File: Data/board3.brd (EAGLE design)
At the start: 70 x 67.5 mm, 69 parts, among them Q1 16MHz, U1 ACPL224, U10 PIC18F46K22-I/PT, U11 MAX3232CSE, U12 ACPL224, U13 VO1400, U14 VO1400, U15 VO1400, U16 VO1400, U17 VO1400, U18 VO1400, U2 ACPL224, U3 ACPL224, U4 ACPL224, U5 VO1400, U6 VO1400, U7 VO1400, U8 VO1400, U9 MCP17033302I/MB, X1 2514-5, X2 2514-5

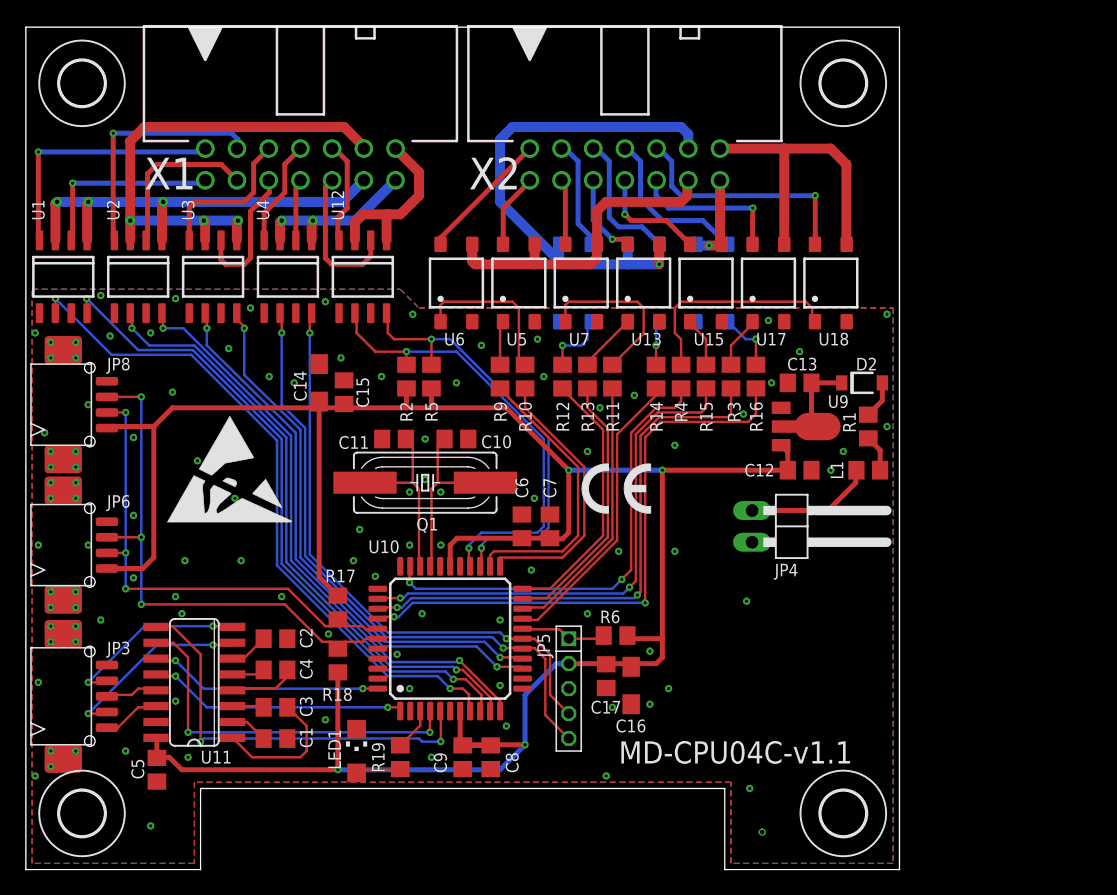
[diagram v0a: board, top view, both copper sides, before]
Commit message: Millores en la deteccio d'error del importador eagle
Signed-off-by: Rafael Serrano <rsr.private@gmail.com>
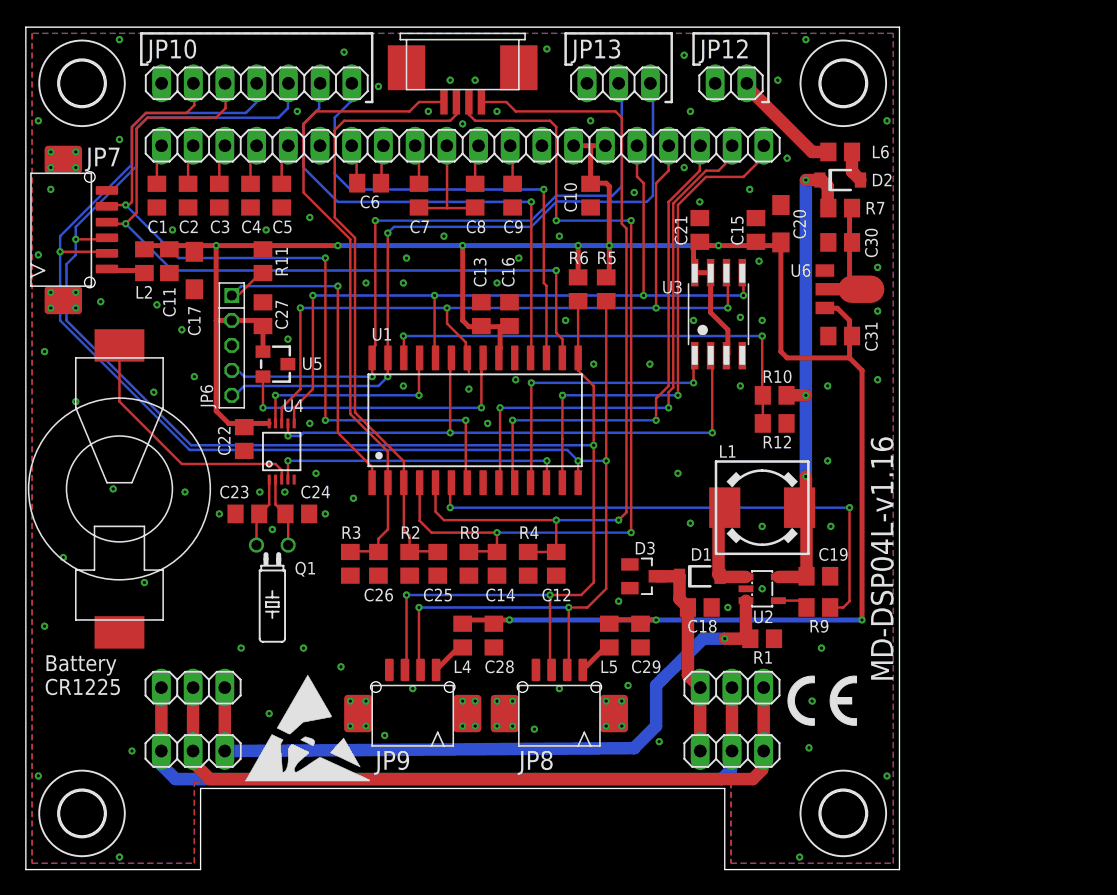
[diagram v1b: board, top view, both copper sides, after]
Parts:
- removed LED1: GREEN, led:CHIPLED_1206
- removed R13, R14, R15, R16, R19: 270, rcl:R0805
- removed R17, R18: 1K5, rcl:R0805
- removed U$10, U$9: (no value), holes:3,6
- removed U10: PIC18F46K22-I/PT, microchip-pic:TQFP44
- removed U11: MAX3232CSE, maxim:SO16
- removed U12: ACPL224, optoacopladores:SO08
- removed U13, U14, U15, U16, U17, U18, U7, U8: VO1400, optoacopladores:SOP04
- removed U9: MCP17033302I/MB, microchip-analog:SOT89
- removed X1, X2: 2514-5, con-3m:PAK100/2500-5-14
- added BAT1: CR1225, bateries:SMTU-1225-1
- added C18: 1u/25V, rcl:C0805
- added C19: 10u, rcl:C0805
- added C20: 10u/6.3V, rcl:SMC_A
- added C21, C22, C25, C26, C27, C28, C29: 100n, rcl:C0805
- added C23, C24: 8p, rcl:C0805
- added C30, C31: 4u7, rcl:C0805
- added D1: MBR0540, diode:SOD123FL
- added D3: BZX84C24, diode:SOT23
- added JP1: (no value), pinhead:1X20
- added JP10: (no value), pinhead:1X07
- added JP11: (no value), te-connector-fpc:FPC-ZB4-1MM
- added JP12: (no value), pinhead:1X02
- added JP13, JP2: (no value), pinhead:1X03
- added JP7: DF13-1X6-SMD-90-E, hirose-df13:1X6-SMD-90-E
- added JP9: DF13-1X4-SMD-90-E, hirose-df13:1X4-SMD-90-E
- added L2, L4, L5, L6: 600R, rcl-2:L0805
- added R7: 5R, rcl:R0805
- added R8: 47k, rcl:R0805
- added U$4: (no value), holes:3,6
- added U$5: (no value), logo:CE-4MM
- C1, C2, C3, C4, C5, C7, C9: value 100n -> 1u/25V
- C10, C11: value 22p -> 100n
- C12, C13: value 4u7 -> 100n
- C14: value 10u -> 100n; device rcl:SMC_A -> rcl:C0805
- C16: value 10u -> 10n; device rcl:SMC_A -> rcl:C0805
- C17: value 100n -> 10u/6.3V; device rcl:C0805 -> rcl:SMC_A
- C6, C8: value 10n -> 1u/25V
- JP3: value DF13-1X5-SMD-90-E -> (none); device hirose-df13:1X5-SMD-90-E -> pinhead:1X03
- JP4: device pinhead:1X02/90 -> pinhead:1X03
- JP5: value ICSP -> (none); device pinhead200:1X05-2MM -> pinhead:1X03
- JP6: value DF13-1X4-SMD-90-E -> PINHD-1X5-2MM; device hirose-df13:1X4-SMD-90-E -> pinhead200:1X05-2MM
- L1: value 600R -> (none); device rcl-2:L0805 -> inductors:DR73
- Q1: value 16MHz -> 32Khz; device crystal:SM49 -> crystal:TC26H
- R1: value 5R1 -> 6R98
- R10, R9: value 270 -> 4K7
- R11: value 270 -> 10K
- R12: value 270 -> 1K5
- R2: value 10K -> 47k
- R3, R4: value 270 -> 47k
- R5, R6: value 10K -> 1K5
- U$1: device logo:CE-4MM -> holes:3,6
- U$2: device logo:ESD_10.00 -> holes:3,6
- U$6: device holes:3,6 -> logo:ESD_10.00
- U1: value ACPL224 -> PIC18F26K22-I/SO; device optoacopladores:SO08 -> microchip-pic:SO28W
- U2: value ACPL224 -> (none); device optoacopladores:SO08 -> onsemiconductor:SOT23-5L
- U3: value ACPL224 -> 25LC1024-I/SM; device optoacopladores:SO08 -> microchip-smem:SO08M
- U4: value ACPL224 -> MCP79520-I/MS; device optoacopladores:SO08 -> microchip-rtc:SO10
- U5: value VO1400 -> TC1047; device optoacopladores:SOP04 -> microchip-analog:TO236
- U6: value VO1400 -> MCP17033302I/MB; device optoacopladores:SOP04 -> microchip-analog:SOT89
- moved U$6 73.8 mm to (17.5, 7.00)
- moved U2 55.9 mm to (59.0, 22.5), turned to 270 degrees
- moved U$1 52.8 mm to (4.50, 63.0)
- moved JP4 51.8 mm to (13.4, 9.50), turned to 0 degrees
- moved JP3 50.2 mm to (56.6, 9.50), turned to 0 degrees
- moved C5 47.1 mm to (20.5, 54.0)
- moved C17 46.3 mm to (13.5, 48.0), turned to 270 degrees
- moved C9 45.2 mm to (39.0, 54.0)
- moved C8 45.0 mm to (36.0, 54.0), turned to 270 degrees
- moved C1 44.5 mm to (10.5, 54.0), turned to 90 degrees
- moved JP8 42.0 mm to (42.8, 16.0), turned to 180 degrees
- moved C3 41.2 mm to (15.5, 54.0), turned to 90 degrees
- moved U3 40.6 mm to (55.5, 44.5), turned to 0 degrees
- moved C4 38.1 mm to (18.0, 54.0), turned to 90 degrees
- moved C2 36.2 mm to (13.0, 54.0), turned to 90 degrees
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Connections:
- removed net I-COM0: U1.1, U1.3, U2.1, X1.11
- removed net I-COM1: U2.3, U3.1, U3.3, X1.12
- removed net I-COM2: U4.1, U4.3, X1.13
- removed net I-COM3: U12.1, U12.3, X1.14
- removed net I0: U1.2, X1.1
- removed net I1: U1.4, X1.2
- removed net I2: U2.2, X1.3
- removed net I3: U2.4, X1.4
- removed net I4: U3.2, X1.5
- removed net I5: U3.4, X1.6
- removed net I6: U4.2, X1.7
- removed net I7: U4.4, X1.8
- removed net I8: U12.2, X1.9
- removed net I9: U12.4, X1.10
- removed net IN0: U1.8, U10.9
- removed net IN1: U1.6, U10.8
- removed net IN2: U10.11, U2.8
- removed net IN3: U10.10, U2.6
- removed net IN4: U10.15, U3.8
- removed net IN5: U10.14, U3.6
- removed net IN6/PGD: JP5.4, U10.17, U4.8
- removed net IN7/PGC: JP5.5, U10.16, U4.6
- removed net IN8: R5.1, U10.25, U12.8
- removed net IN9: R2.1, U10.26, U12.6
- removed net LED: R19.2, U10.3
- removed net N$30: C4.2, U11.4
- removed net N$33: C4.1, U11.5
- removed net N$34: C1.1, U11.2
- removed net N$35: C2.1, U11.6
- removed net N$36: C11.2, Q1.2, U10.31
- removed net N$51: R15.2, U15.1
- removed net N$52: R13.2, U13.1
- removed net N$53: R14.2, U14.1
- removed net N$54: R16.2, U16.1
- removed net O-COM0: U5.3, U6.3, U7.3, X2.11
- removed net O-COM1: U13.3, U14.3, U8.3, X2.12
- removed net O-COM2: U15.3, U16.3, X2.13
- removed net O-COM3: U17.3, U18.3, X2.14
- removed net O0: U5.4, X2.1
- removed net O1: U6.4, X2.2
- removed net O2: U7.4, X2.3
- removed net O3: U8.4, X2.4
- removed net O4: U13.4, X2.5
- removed net O5: U14.4, X2.6
- removed net O6: U15.4, X2.7
- removed net O7: U16.4, X2.8
- removed net O8: U17.4, X2.9
- removed net O9: U18.4, X2.10
- removed net OUT0: R9.1, U10.24
- removed net OUT1: R10.1, U10.23
- removed net OUT2: R11.1, U10.20
- removed net OUT3: R12.1, U10.22
- removed net OUT4: R13.1, U10.21
- removed net OUT5: R14.1, U10.19
- removed net OUT6: R15.1, U10.35
- removed net OUT7: R16.1, U10.37
- removed net OUT8: R3.1, U10.36
- removed net OUT9: R4.1, U10.32
- removed net SCL2: JP6.2, JP8.2, R17.1, U10.38
- removed net SDA2: JP6.3, JP8.3, R18.1, U10.39
- new net +5V: C19.1, D2.C, L1.1, R10.2, R7.2, U2.5
- new net A+: C12.1, JP11.1, R4.2, U1.5
- new net A-: C25.1, JP11.3, R2.2, U1.3
- new net A0-DSP: JP1.18, U1.10
- new net B+: C14.1, JP11.2, R8.2, U1.4
- new net B-: C26.1, JP11.4, R3.2, U1.2
- new net BK_EN: R9.2, U1.6
- new net CS-DSP: JP1.20, U1.13
- new net CS-MEM: U1.11, U3.1
- new net CS-RTC: U1.12, U4.4
- new net MFP-RTC: U1.25, U4.9
- new net MISO: U1.23, U3.2, U4.7
- new net MOSI: JP1.16, U1.24, U3.5, U4.6
- new net N$10: C7.2, C8.2, JP1.10
- new net N$11: C8.1, JP1.11
- new net N$12: C9.2, JP1.12
- new net N$19: D1.A, L1.2, U2.1
- new net N$21: JP7.1, L2.2
- new net N$24: D2.A, L6.2
- new net N$27: C30.1, R7.1, U6.2, U6.2@1
- new net N$9: C7.1, JP1.9
- new net RST-DSP: JP1.19, U1.9
- new net SCK: JP1.17, U1.22, U3.6, U4.8
- new net SCL/SCK: JP10.4, JP7.2, JP8.2, JP9.2, R5.1, U1.14
- new net SDA/SDI: JP10.3, JP7.3, JP8.3, JP9.3, R6.1, U1.15
- new net SDO: JP10.5, JP7.4, U1.16
- new net SS: JP10.6, JP7.5, U1.7
- new net VPOWER: R10.1, R12.2, U1.26
- new net VTEMP: U1.21, U5.2
- net GND: now also BAT1.NEG, C1.1, C10.2, C11.2, C14.2, C15.2, C16.2, C17.-, C18.2, C19.2, C2.1, C20.-, C21.2, C22.2, C23.2, C24.2, C25.2, C26.2, C27.2, C28.2, C29.2, C3.1, C30.2, C31.2, C4.1, D3.1, JP1.13, JP1.6, JP10.7, JP12.2, JP13.3, JP6.3, JP7.6, JP9.4, R1.1, R12.1, R2.1, R3.1, R4.1, R8.1, U1.19, U1.8, U2.2, U3.4, U5.3, U6.1; no longer C1.2, C10.1, C11.1, C14.-, C15.1, C16.-, C17.1, C2.2, C6.1, C7.1, C8.1, JP3.5, JP4.2, JP5.3, JP6.4, LED1.C, U1.5, U1.7, U10.29, U10.6, U11.15, U12.5, U12.7, U13.2, U14.2, U15.2, U16.2, U17.2, U18.2, U2.5, U2.7, U3.5, U3.7, U4.7, U5.2, U6.2, U7.2, U8.2, U9.1
- net N$1: now also C1.2, JP1.1; no longer R3.2, U17.1
- net N$13: now also JP2.2, JP4.1, JP5.1; no longer U11.7
- net N$14: now also JP4.3, JP5.3, R1.2, U2.3; no longer JP3.3, U11.13
- net N$15: now also BAT1.POS, U4.3; no longer JP3.4, U11.8
- net N$16: now also C18.1, D1.C, D3.3, JP2.1, JP3.1; no longer C3.2, U11.1
- net N$17: now also C23.1, Q1.2, U4.1; no longer R9.2, U5.1
- net N$18: now also C24.1, Q1.1, U4.2; no longer R10.2, U6.1
- net N$2: now also C2.2, JP1.2; no longer JP4.1, L1.2
- net N$22: now also JP12.1, L6.1; no longer LED1.A, R19.1
- net N$25: now also JP9.1, L4.2; no longer R11.2, U7.1
- net N$26: now also JP8.1, L5.2; no longer R12.2, U8.1
- net N$29: now also R9.1, U2.4; no longer C3.1, U11.3
- net N$3: now also C3.2, JP1.3; no longer L1.1, R1.1
- net N$4: now also C4.2, JP1.4; no longer JP3.1, U11.14
- net N$5: now also C5.2, JP1.5; no longer C13.1, D2.C, U9.2, U9.2@1
- net N$6: now also JP2.3, JP3.3, JP4.2, JP5.2; no longer R4.2, U18.1
- net N$7: now also C6.2, JP1.7; no longer D2.A, R1.2
- net N$8: now also C6.1, JP1.8; no longer C10.2, Q1.1, U10.30
- net RX1: now also JP10.2, U1.18; no longer U10.1, U11.12
- net RX2: now also JP13.2, JP6.4, U1.28; no longer U10.5, U11.9
- net TX1: now also JP10.1, U1.17; no longer U10.44, U11.11
- net TX2: now also JP13.1, JP6.5, U1.27; no longer U10.4, U11.10
- net VCC: now also C10.1, C11.1, C13.1, C15.1, C16.1, C17.+, C20.+, C21.1, C22.1, C27.1, C28.1, C29.1, C31.1, JP1.14, JP1.15, JP6.2, L2.1, L4.1, L5.1, R11.2, U1.20, U3.3, U3.7, U3.8, U4.10, U5.1, U6.3; no longer C12.1, C14.+, C15.2, C16.+, C17.2, C5.2, C6.2, C7.2, C8.2, C9.2, JP5.2, JP6.1, JP8.1, R17.2, R18.2, R2.2, U10.28, U10.7, U11.16, U9.3
- net VPP: now also JP6.1, R11.1, U1.1; no longer JP5.1, R6.1, U10.18
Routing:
- net SDA/SDI: track 0.00 -> 133.5 mm, vias 0 -> 4
- net SCL/SCK: track 0.00 -> 132.9 mm, vias 0 -> 5
- net B+: track 0.00 -> 71.2 mm, vias 0 -> 4
- net SCK: track 0.00 -> 67.4 mm, vias 0 -> 4
- net A+: track 0.00 -> 66.5 mm, vias 0 -> 2
- net MOSI: track 0.00 -> 64.5 mm, vias 0 -> 4
- net SS: track 0.00 -> 62.7 mm, vias 0 -> 4
- net SDO: track 0.00 -> 62.6 mm, vias 0 -> 2
- net IN1: track 54.7 -> 0.00 mm, vias 2 -> 0
- net IN0: track 53.4 -> 0.00 mm, vias 2 -> 0
- net B-: track 0.00 -> 52.3 mm
- net N$14: track 4.24 -> 55.9 mm, vias 0 -> 1
- net A-: track 0.00 -> 50.7 mm
- net IN7/PGC: track 50.7 -> 0.00 mm, vias 2 -> 0
- net IN3: track 50.3 -> 0.00 mm, vias 2 -> 0
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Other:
- board text added: "Battery CR1225"
- board text added: "MD-DSP04L-v1.16"
- board text removed: "MD-CPU04C-v1.1"

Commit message: Implementacio GetOutline per l'element regio.
Signed-off-by: Rafael Serrano <rsr.private@gmail.com>
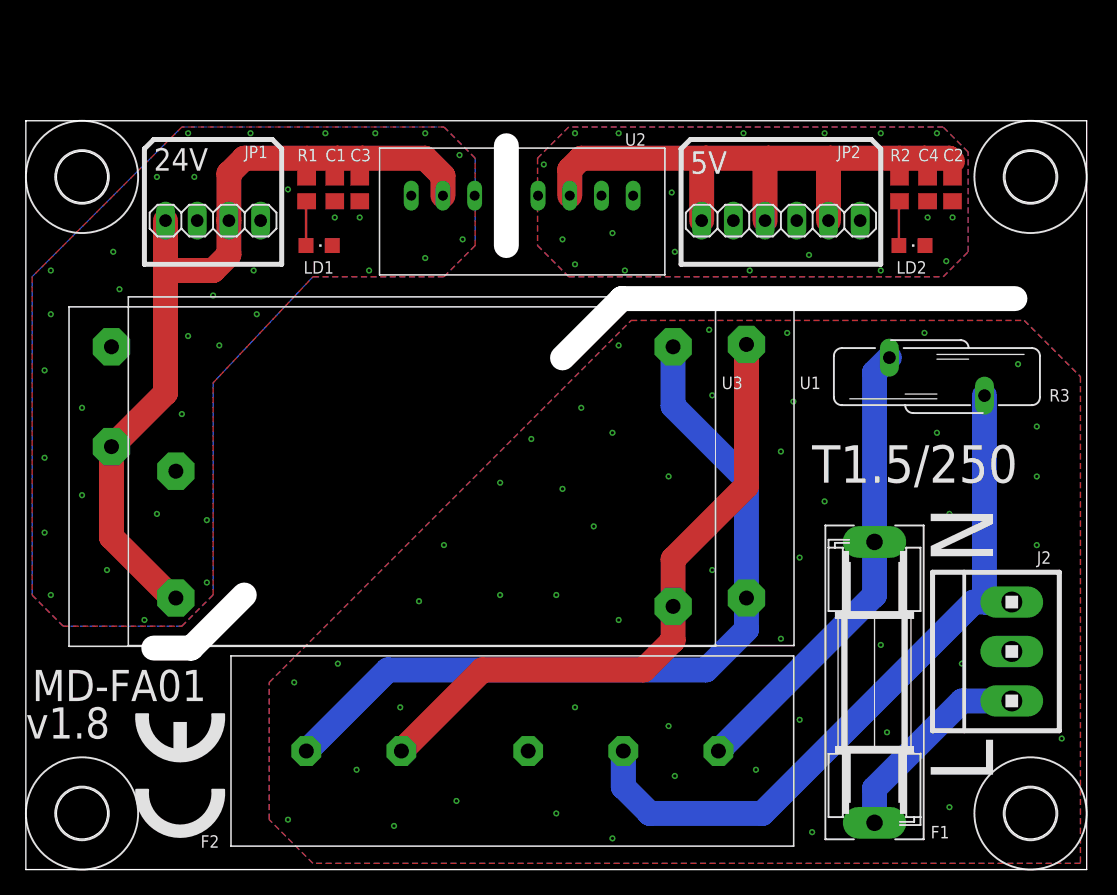
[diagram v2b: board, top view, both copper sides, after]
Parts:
- removed BAT1: CR1225, bateries:SMTU-1225-1
- removed C10, C11, C12, C13, C14, C15, C21, C22, C25, C26, C27, C28, C29: 100n, rcl:C0805
- removed C16: 10n, rcl:C0805
- removed C17, C20: 10u/6.3V, rcl:SMC_A
- removed C18, C5, C6, C7, C8, C9: 1u/25V, rcl:C0805
- removed C19: 10u, rcl:C0805
- removed C23, C24: 8p, rcl:C0805
- removed C30, C31: 4u7, rcl:C0805
- removed D1, D2: MBR0540, diode:SOD123FL
- removed D3: BZX84C24, diode:SOT23
- removed JP10: (no value), pinhead:1X07
- removed JP11: (no value), te-connector-fpc:FPC-ZB4-1MM
- removed JP12: (no value), pinhead:1X02
- removed JP13, JP3, JP4, JP5: (no value), pinhead:1X03
- removed JP6: PINHD-1X5-2MM, pinhead200:1X05-2MM
- removed JP7: DF13-1X6-SMD-90-E, hirose-df13:1X6-SMD-90-E
- removed JP8, JP9: DF13-1X4-SMD-90-E, hirose-df13:1X4-SMD-90-E
- removed L1: (no value), inductors:DR73
- removed L2, L4, L5, L6: 600R, rcl-2:L0805
- removed Q1: 32Khz, crystal:TC26H
- removed R10, R9: 4K7, rcl:R0805
- removed R11: 10K, rcl:R0805
- removed R12, R5, R6: 1K5, rcl:R0805
- removed R4, R8: 47k, rcl:R0805
- removed R7: 5R, rcl:R0805
- removed U$4: (no value), holes:3,6
- removed U4: MCP79520-I/MS, microchip-rtc:SO10
- removed U5: TC1047, microchip-analog:TO236
- removed U6: MCP17033302I/MB, microchip-analog:SOT89
- added F1: T1.5A/250, fuse:SH22,5
- added F2: FN-406-05-02, schaffner:FN-406
- added J2: (no value), con-amp:1X3MTA
- added LD1, LD2: HSMS-C170, led:CHIPLED_0805
- C1, C4: value 1u/25V -> 100n/50V
- C2, C3: value 1u/25V -> 10n/50V
- JP1: device pinhead:1X20 -> pinhead:1X04
- JP2: device pinhead:1X03 -> pinhead:1X06
- R1: value 6R98 -> 4K3
- R2: value 47k -> 560
- R3: value 47k -> S14K250; device rcl:R0805 -> varistor:S14K250
- U$1, U$2, U$3: device holes:3,6 -> holes:4,1
- U$5: device logo:CE-4MM -> logo:CE_10.00
- U$6: device logo:ESD_10.00 -> holes:4,1
- U1: value PIC18F26K22-I/SO -> RAC10-24SC/227; device microchip-pic:SO28W -> recom:RAC10-SB
- U2: value (none) -> RS-2405S; device onsemiconductor:SOT23-5L -> recom:RS
- U3: value 25LC1024-I/SM -> IRM-20-24; device microchip-smem:SO08M -> meanwell:IRM-20
- moved U$6 79.5 mm to (80.5, 55.5)
- moved C2 61.3 mm to (74.2, 54.5), turned to 270 degrees
- moved C4 54.3 mm to (72.2, 54.5), turned to 270 degrees
- moved R1 51.3 mm to (22.5, 54.5), turned to 90 degrees
- moved R2 49.4 mm to (70.0, 54.5)
- moved R3 49.3 mm to (73.0, 39.5)
- moved U$5 45.9 mm to (16.0, 2.50), turned to 90 degrees
- moved JP2 37.6 mm to (60.5, 52.0)
- moved U2 37.6 mm to (38.5, 54.0), turned to 0 degrees
- moved U3 29.6 mm to (29.0, 31.2)
- moved JP1 20.9 mm to (15.0, 52.0)
- moved U$3 15.0 mm to (80.5, 4.50)
- moved C1 14.3 mm to (24.8, 54.5), turned to 270 degrees
- moved C3 11.3 mm to (26.8, 54.5), turned to 270 degrees
- moved U$1 7.50 mm to (4.50, 55.5)
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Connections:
- removed net +5V: C19.1, D2.C, L1.1, R10.2, R7.2, U2.5
- removed net A+: C12.1, JP11.1, R4.2, U1.5
- removed net A-: C25.1, JP11.3, R2.2, U1.3
- removed net A0-DSP: JP1.18, U1.10
- removed net B+: C14.1, JP11.2, R8.2, U1.4
- removed net B-: C26.1, JP11.4, R3.2, U1.2
- removed net BK_EN: R9.2, U1.6
- removed net CS-DSP: JP1.20, U1.13
- removed net CS-MEM: U1.11, U3.1
- removed net CS-RTC: U1.12, U4.4
- removed net GND: BAT1.NEG, C1.1, C10.2, C11.2, C12.2, C13.2, C14.2, C15.2, C16.2, C17.-, C18.2, C19.2, C2.1, C20.-, C21.2, C22.2, C23.2, C24.2, C25.2, C26.2, C27.2, C28.2, C29.2, C3.1, C30.2, C31.2, C4.1, C5.1, C9.1, D3.1, JP1.13, JP1.6, JP10.7, JP12.2, JP13.3, JP6.3, JP7.6, JP8.4, JP9.4, R1.1, R12.1, R2.1, R3.1, R4.1, R8.1, U1.19, U1.8, U2.2, U3.4, U4.5, U5.3, U6.1
- removed net MFP-RTC: U1.25, U4.9
- removed net MISO: U1.23, U3.2, U4.7
- removed net MOSI: JP1.16, U1.24, U3.5, U4.6
- removed net N$1: C1.2, JP1.1
- removed net N$10: C7.2, C8.2, JP1.10
- removed net N$11: C8.1, JP1.11
- removed net N$12: C9.2, JP1.12
- removed net N$13: JP2.2, JP3.2, JP4.1, JP5.1
- removed net N$14: JP4.3, JP5.3, R1.2, U2.3
- removed net N$15: BAT1.POS, U4.3
- removed net N$16: C18.1, D1.C, D3.3, JP2.1, JP3.1
- removed net N$17: C23.1, Q1.2, U4.1
- removed net N$18: C24.1, Q1.1, U4.2
- removed net N$19: D1.A, L1.2, U2.1
- removed net N$2: C2.2, JP1.2
- removed net N$21: JP7.1, L2.2
- removed net N$22: JP12.1, L6.1
- removed net N$24: D2.A, L6.2
- removed net N$25: JP9.1, L4.2
- removed net N$26: JP8.1, L5.2
- removed net N$27: C30.1, R7.1, U6.2, U6.2@1
- removed net N$29: R9.1, U2.4
- removed net N$3: C3.2, JP1.3
- removed net N$5: C5.2, JP1.5
- removed net RST-DSP: JP1.19, U1.9
- removed net RX1: JP10.2, U1.18
- removed net RX2: JP13.2, JP6.4, U1.28
- removed net SCK: JP1.17, U1.22, U3.6, U4.8
- removed net SCL/SCK: JP10.4, JP7.2, JP8.2, JP9.2, R5.1, U1.14
- removed net SDA/SDI: JP10.3, JP7.3, JP8.3, JP9.3, R6.1, U1.15
- removed net SDO: JP10.5, JP7.4, U1.16
- removed net SS: JP10.6, JP7.5, U1.7
- removed net TX1: JP10.1, U1.17
- removed net TX2: JP13.1, JP6.5, U1.27
- removed net VCC: C10.1, C11.1, C13.1, C15.1, C16.1, C17.+, C20.+, C21.1, C22.1, C27.1, C28.1, C29.1, C31.1, JP1.14, JP1.15, JP6.2, L2.1, L4.1, L5.1, R11.2, R5.2, R6.2, U1.20, U3.3, U3.7, U3.8, U4.10, U5.1, U6.3
- removed net VPOWER: R10.1, R12.2, U1.26
- removed net VPP: JP6.1, R11.1, U1.1
- removed net VTEMP: U1.21, U5.2
- new net FL: F2.P$5, U1.2, U3.2
- new net FN: F2.P$4, U1.1, U3.1
- new net GND-V24: C1.2, C3.2, JP1.2, JP1.4, LD1.C, U1.4, U2.1, U3.3
- new net GND-V3.3: C2.2, C4.2, JP2.2, JP2.4, JP2.6, LD2.C, U2.7
- new net PE: F2.P$3, J2.2
- new net V24: C1.1, C3.1, JP1.1, JP1.3, R1.2, U1.3, U2.2, U3.4
- new net V3.3: C2.1, C4.1, JP2.1, JP2.3, JP2.5, R2.2, U2.6
- net N$4: now also LD1.A, R1.1; no longer C4.2, JP1.4
- net N$6: now also LD2.A, R2.1; no longer JP2.3, JP3.3, JP4.2, JP5.2
- net N$7: now also F1.2, F2.P$1, R3.2; no longer C6.2, JP1.7
- net N$8: now also F2.P$2, J2.1, R3.1; no longer C6.1, JP1.8
- net N$9: now also F1.1, J2.3; no longer C7.1, JP1.9
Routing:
- net VCC: track 202.8 -> 0.00 mm, vias 9 -> 0
- net SDA/SDI: track 133.5 -> 0.00 mm, vias 4 -> 0
- net SCL/SCK: track 132.9 -> 0.00 mm, vias 5 -> 0
- net B+: track 71.2 -> 0.00 mm, vias 4 -> 0
- net V24: track 0.00 -> 71.1 mm
- net SCK: track 67.4 -> 0.00 mm, vias 4 -> 0
- net A+: track 66.5 -> 0.00 mm, vias 2 -> 0
- net MOSI: track 64.5 -> 0.00 mm, vias 4 -> 0
- net FN: track 0.00 -> 64.4 mm
- net SS: track 62.7 -> 0.00 mm, vias 4 -> 0
- net SDO: track 62.6 -> 0.00 mm, vias 2 -> 0
- net N$13: track 59.6 -> 0.00 mm
- net TX2: track 56.2 -> 0.00 mm, vias 2 -> 0
- net N$14: track 55.9 -> 0.00 mm, vias 1 -> 0
- net N$6: track 59.1 -> 3.56 mm
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- added copper zone on layer 1, net GND-V24
- added copper zone on layer 16, net GND-V24
- added copper zone on layer 1, net GND-V3.3
- added copper zone on layer 16, net GND-V3.3
- added copper zone on layer 1, net PE
- added copper zone on layer 16, net PE
- removed copper zone on layer 1, net GND
- removed copper zone on layer 16, net GND
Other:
- board size 70 x 67.5 mm -> 85 x 60 mm
- board text added: "24V"
- board text added: "5V"
- board text added: "DANGER HIGH VOLTAGE"
- board text added: "L"
- board text added: "MD-FA01"
- board text added: "N"
- board text added: "T1.5/250"
- board text added: "v1.8"
- board text removed: "Battery CR1225"
- board text removed: "MD-DSP04L-v1.16"
